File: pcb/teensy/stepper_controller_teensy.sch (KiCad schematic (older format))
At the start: 8 parts, among them SW1 SPST_SLIDE_AS

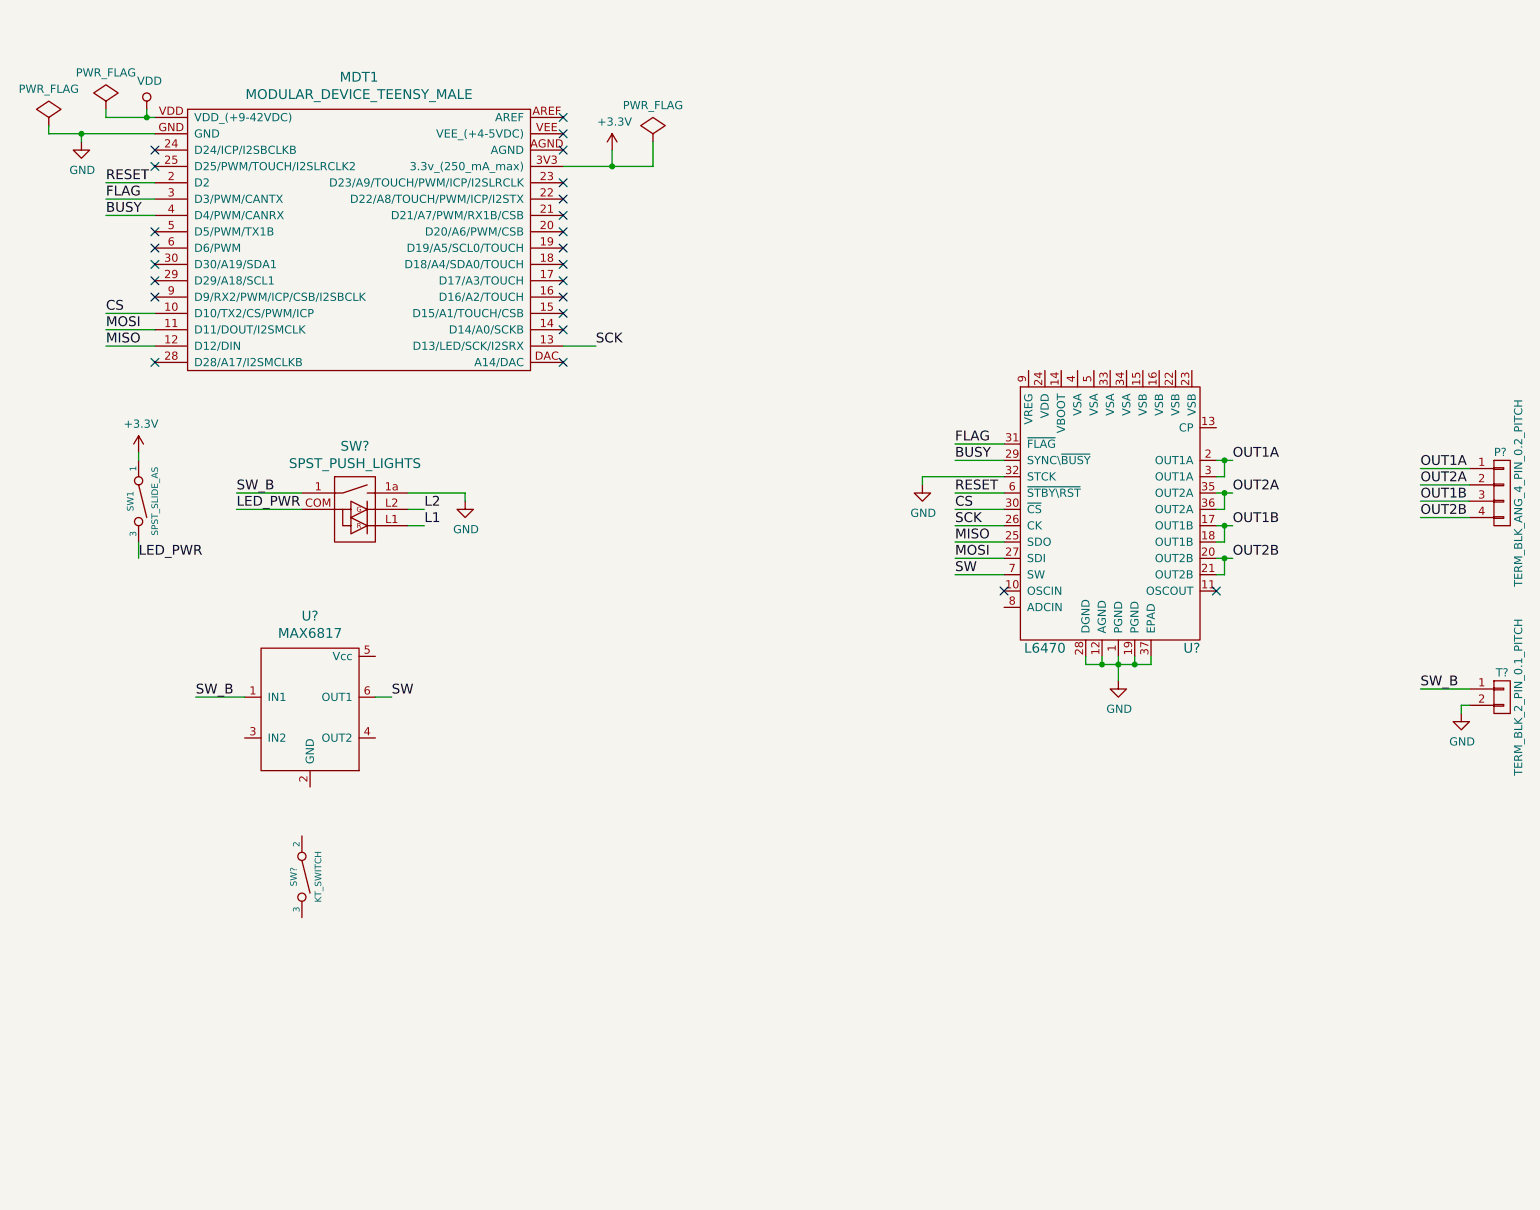
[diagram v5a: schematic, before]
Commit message: Progress towards teensy pcb v1.0.
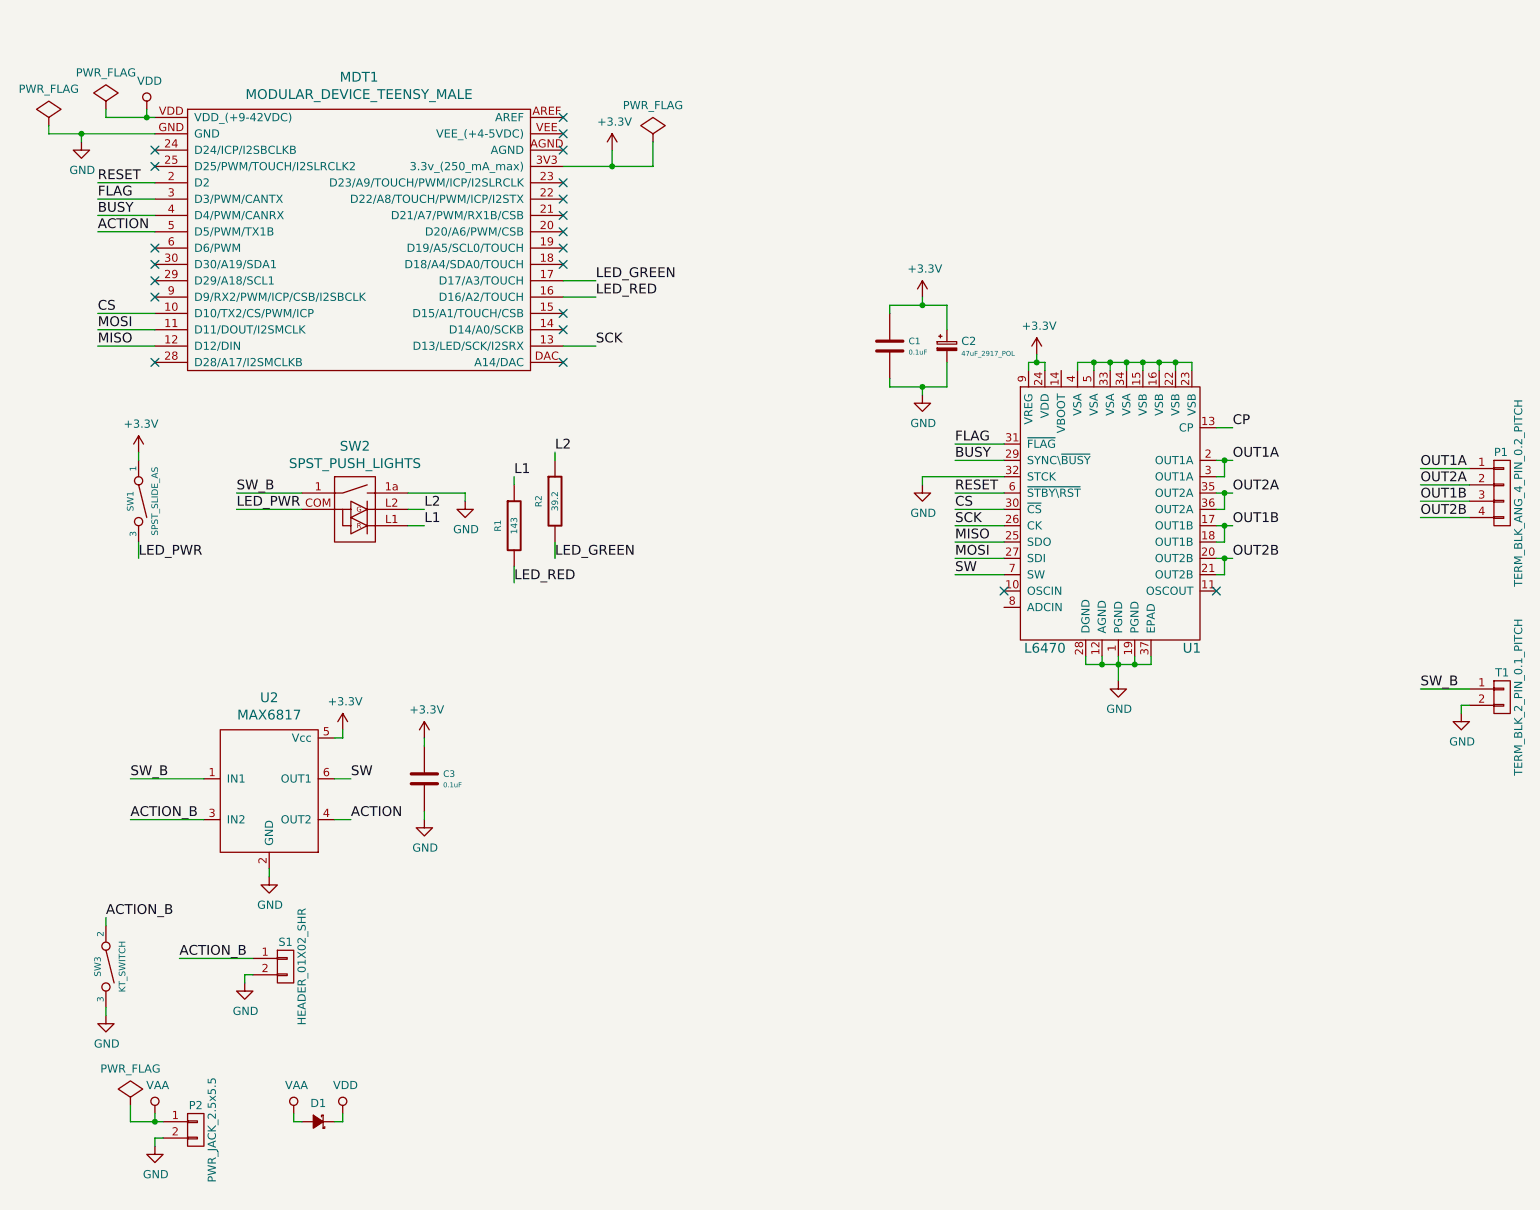
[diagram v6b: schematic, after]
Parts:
- removed U?: L6470, footprints:POWERSO-36, symbol L6470
- added C1, C3: 0.1uF, footprints:SM1210, symbol 0.1uF
- added C2: 47uF_2917_POL, footprints:SM2917_POL, symbol 47uF_2917_POL
- added D1: diode_schottky_45V_10A, footprints:CFP15, symbol diode_schottky_45V_10A
- added P2: PWR_JACK_2.5x5.5, footprints:DCJACK_2PIN_HIGHCURRENT, symbol PWR_JACK_2.5x5.5
- added R1: 143, footprints:SM1210, symbol 143
- added R2: 39.2, footprints:SM1210, symbol 39.2
- added S1: HEADER_01X02_SHR, footprints:Header_Shrouded_2_Pin, symbol HEADER_01X02_SHR
- added U1: L6470, footprints:POWERSO-36, symbol L6470
- gave numbers to parts that had none: 5
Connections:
- net +3V3: now also U2.5 (Vcc), C1.1, C2.1, C3.1, U1.24 (VDD), U1.9 (VREG)
- net BUSY: now also U1.29 (SYNC\~BUSY)
- net CS: now also U1.30 (~CS)
- net FLAG: now also U1.31 (~FLAG)
- net GND: now also SW3.3, U2.2 (GND), C1.2, C2.2, C3.2, P2.2 (P2), S1.2 (P2), U1.1 (PGND), U1.12 (AGND), U1.19 (PGND), U1.28 (DGND), U1.32 (STCK), U1.37 (EPAD)
- net L1: now also R1.1
- net L2: now also R2.1
- net MISO: now also U1.25 (SDO)
- net MOSI: now also U1.27 (SDI)
- net OUT1A: now also U1.2 (OUT1A), U1.3 (OUT1A)
- net OUT1B: now also U1.17 (OUT1B), U1.18 (OUT1B)
- net OUT2A: now also U1.35 (OUT2A), U1.36 (OUT2A)
- net OUT2B: now also U1.20 (OUT2B), U1.21 (OUT2B)
- net RESET: now also U1.6 (~STBY\RST)
- net SCK: now also U1.26 (CK)
- net SW: now also U1.7 (SW)
- net VDD: now also D1.1 (K)
- net LED_RED: now reaches MDT1.16 (D16/A2/TOUCH)
- net LED_RED: now also R1.2
- net LED_GREEN: now reaches MDT1.17 (D17/A3/TOUCH)
- net LED_GREEN: now also R2.2
- net ACTION: now reaches MDT1.5 (D5/PWM/TX1B)
- net ACTION: now also U2.4 (OUT2)
- net ACTION_B: now reaches SW3.2
- net ACTION_B: now also U2.3 (IN2), S1.1 (P1)
- new net: U1.15 (VSB), U1.16 (VSB), U1.22 (VSB), U1.23 (VSB), U1.33 (VSA), U1.34 (VSA), U1.4 (VSA), U1.5 (VSA)
- new net CP: U1.13 (CP)
- new net VAA: D1.2 (A), P2.1 (P1)
- no-connect marks 24 -> 21
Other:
- moved on the sheet: SW3, U2

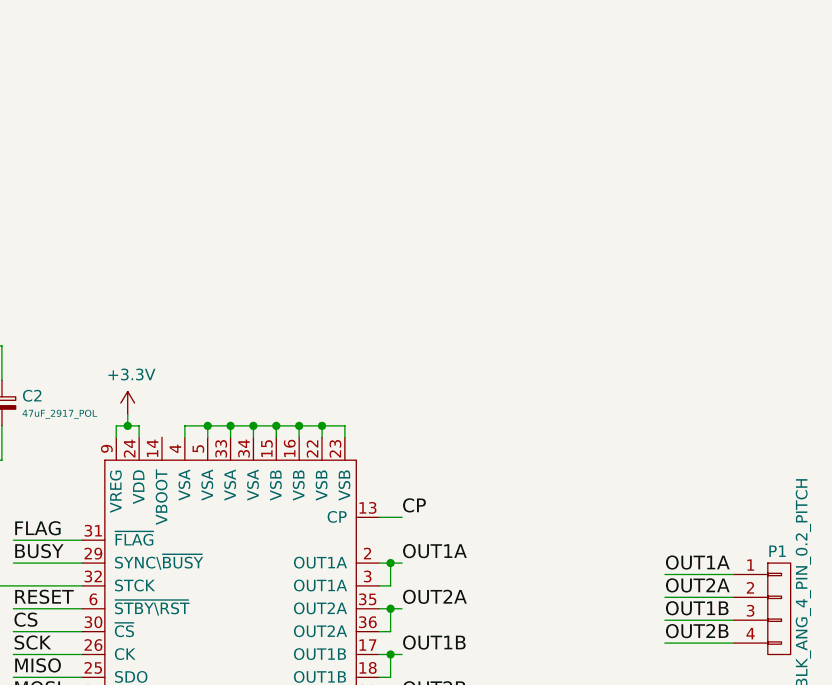
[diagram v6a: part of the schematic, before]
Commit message: Added components.
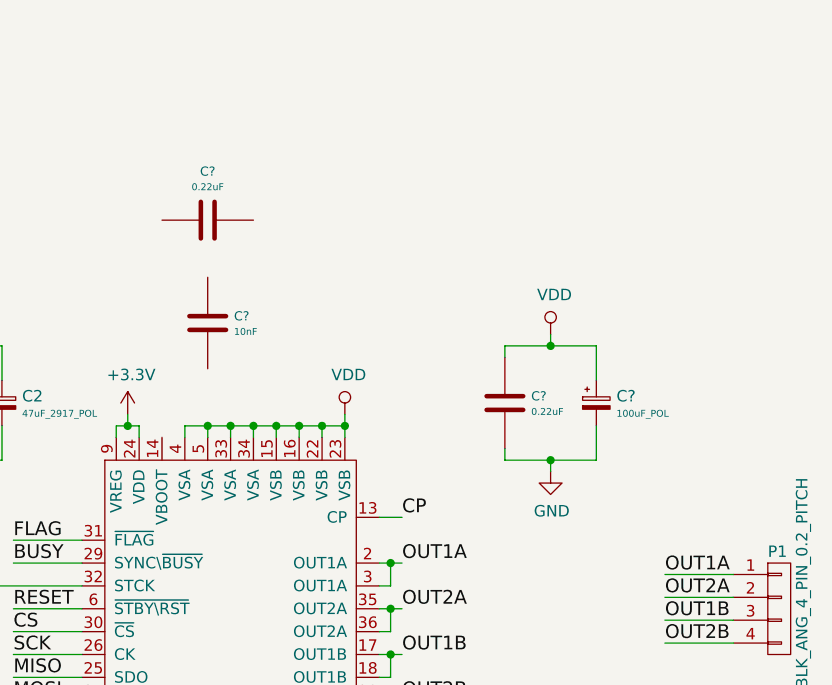
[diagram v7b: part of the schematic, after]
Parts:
- added C?: 10nF, footprints:SM1210, symbol 10nF
- added C? (x2): 0.22uF, footprints:SM1210, symbol 0.22uF
- added C?: 100uF_POL, footprints:C_ELEC_12.5, symbol 100uF_POL
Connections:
- net GND: now also C?.1, C?.2
- net VDD: now also U1.15 (VSB), U1.16 (VSB), U1.22 (VSB), U1.23 (VSB), U1.33 (VSA), U1.34 (VSA), U1.4 (VSA), U1.5 (VSA), C?.1, C?.2
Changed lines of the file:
@@
 	7000 2350 7700 2350
 Wire Wire Line
-	7700 2350 7700 2400
+	7700 2300 7700 2400
 Wire Wire Line
 	7100 2400 7100 2350
@@
 	1    0    0    -1
 $EndComp
+$Comp
+L 10nF C?
+U 1 1 57B49BE4
+P 7100 1900
+F 0 "C?" H 7215 1930 40  0000 L CNN
+F 1 "10nF" H 7215 1862 30  0000 L CNN
+F 2 "footprints:SM1210" H 7138 1750 30  0001 C CNN
+F 3 "" H 7100 1900 60  0000 C CNN
+F 4 "digikey" H 7200 2100 60  0001 C CNN "Vendor"
+F 5 "399-11960-1-ND" H 7300 2200 60  0001 C CNN "PartNumber"
+F 6 "10000pF 100V Ceramic Capacitor C0G NP0 1210" H 7400 2300 60  0001 C CNN "Description"
+	1    7100 1900
+	1    0    0    -1
+$EndComp
+$Comp
+L 0.22uF C?
+U 1 1 57B49D3D
+P 7100 1450
+F 0 "C?" V 6887 1450 40  0000 C CNN
+F 1 "0.22uF" V 6955 1450 30  0000 C CNN
+F 2 "footprints:SM1210" H 7138 1300 30  0001 C CNN
+F 3 "" H 7100 1450 60  0000 C CNN
+F 4 "digikey" H 7200 1650 60  0001 C CNN "Vendor"
+F 5 "399-11615-1-ND" H 7300 1750 60  0001 C CNN "PartNumber"
+F 6 "0.22µF 100V Ceramic Capacitor X7R 1210" H 7400 1850 60  0001 C CNN "Description"
+	1    7100 1450
+	0    1    1    0
+$EndComp
+$Comp
+L 0.22uF C?
+U 1 1 57B49FA3
+P 8400 2250
+F 0 "C?" H 8285 2220 40  0000 R CNN
+F 1 "0.22uF" H 8285 2288 30  0000 R CNN
+F 2 "footprints:SM1210" H 8438 2100 30  0001 C CNN
+F 3 "" H 8400 2250 60  0000 C CNN
+F 4 "digikey" H 8500 2450 60  0001 C CNN "Vendor"
+F 5 "399-11615-1-ND" H 8600 2550 60  0001 C CNN "PartNumber"
+F 6 "0.22µF 100V Ceramic Capacitor X7R 1210" H 8700 2650 60  0001 C CNN "Description"
+	1    8400 2250
+	-1   0    0    1
+$EndComp
+$Comp
+L 100uF_POL C?
+U 1 1 57B4B5B4
+P 8800 2250
+F 0 "C?" H 8888 2280 50  0000 L CNN
+F 1 "100uF_POL" H 8888 2204 30  0000 L CNN
+F 2 "footprints:C_ELEC_12.5" H 8710 2220 60  0001 C CNN
+F 3 "" H 8810 2320 60  0001 C CNN
+F 4 "digikey" H 8910 2420 60  0001 C CNN "Vendor"
+F 5 "565-2511-1-ND" H 9010 2520 60  0001 C CNN "PartNumber"
+F 6 "100µF 100V Aluminum Capacitors Radial Can SMD" H 9110 2620 60  0001 C CNN "Description"
+	1    8800 2250
+	1    0    0    -1
+$EndComp
+Wire Wire Line
+	8400 2450 8400 2500
+Wire Wire Line
+	8400 2500 8800 2500
+Wire Wire Line
+	8800 2500 8800 2350
+Wire Wire Line
+	8400 2050 8400 2000
+Wire Wire Line
+	8400 2000 8800 2000
+Wire Wire Line
+	8800 2000 8800 2150
+$Comp
+L GND #PWR?
+U 1 1 57B4BB86
+P 8600 2550
+F 0 "#PWR?" H 8600 2300 50  0001 C CNN
+F 1 "GND" H 8605 2377 50  0000 C CNN
+F 2 "" H 8600 2550 50  0000 C CNN
+F 3 "" H 8600 2550 50  0000 C CNN
+	1    8600 2550
+	1    0    0    -1
+$EndComp
+$Comp
+L VDD #PWR?
+U 1 1 57B4BC45
+P 8600 1950
+F 0 "#PWR?" H 8600 1800 50  0001 C CNN
+F 1 "VDD" H 8617 2123 50  0000 C CNN
+F 2 "" H 8600 1950 50  0000 C CNN
+F 3 "" H 8600 1950 50  0000 C CNN
+	1    8600 1950
+	1    0    0    -1
+$EndComp
+Wire Wire Line
+	8600 2000 8600 1950
+Connection ~ 8600 2000
+Wire Wire Line
+	8600 2500 8600 2550
+Connection ~ 8600 2500
+$Comp
+L VDD #PWR?
+U 1 1 57B4BF72
+P 7700 2300
+F 0 "#PWR?" H 7700 2150 50  0001 C CNN
+F 1 "VDD" H 7717 2473 50  0000 C CNN
+F 2 "" H 7700 2300 50  0000 C CNN
+F 3 "" H 7700 2300 50  0000 C CNN
+	1    7700 2300
+	1    0    0    -1
+$EndComp
+Connection ~ 7700 2350
 $EndSCHEMATC
